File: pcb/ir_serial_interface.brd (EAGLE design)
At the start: 41.9 x 25.4 mm, 33 parts, among them IC1 PIC18LF2550, IC2 LP2992, T1 PS401

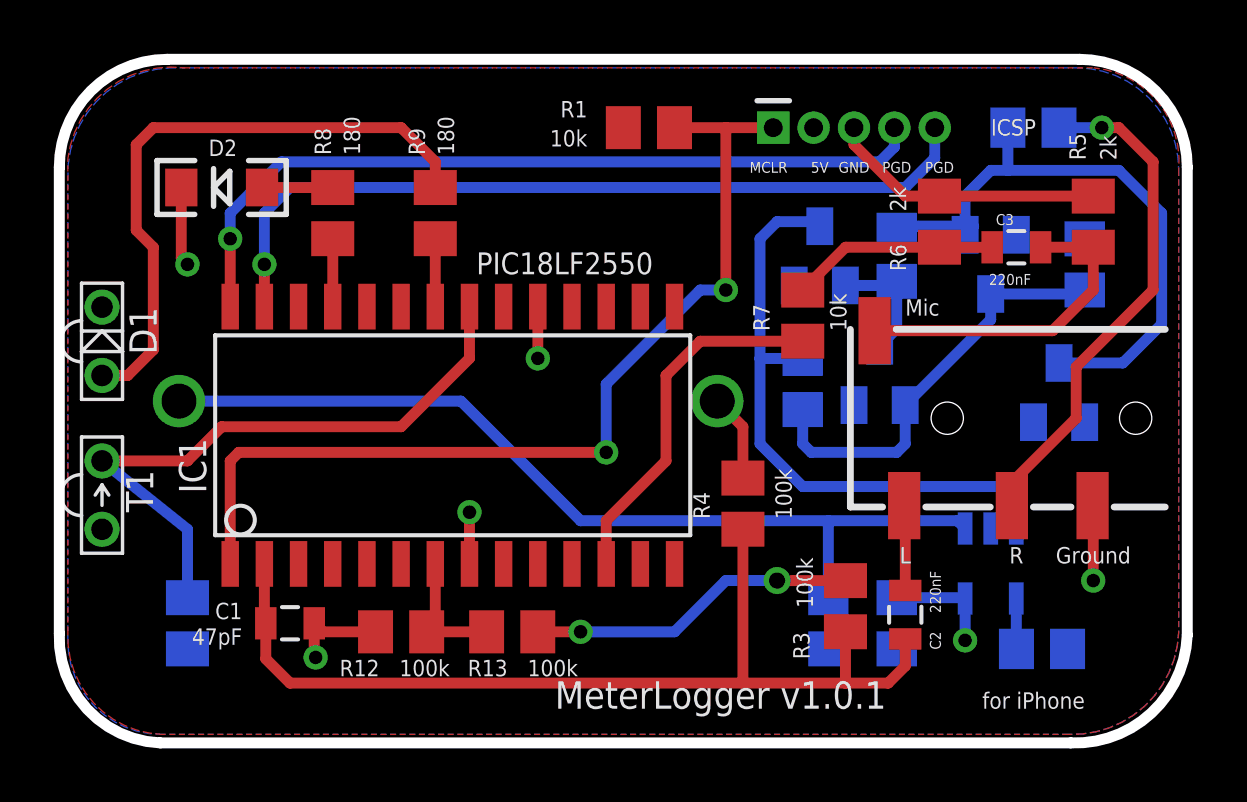
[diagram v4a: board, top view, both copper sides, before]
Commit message: PCB: reuse programmer header for serial debug
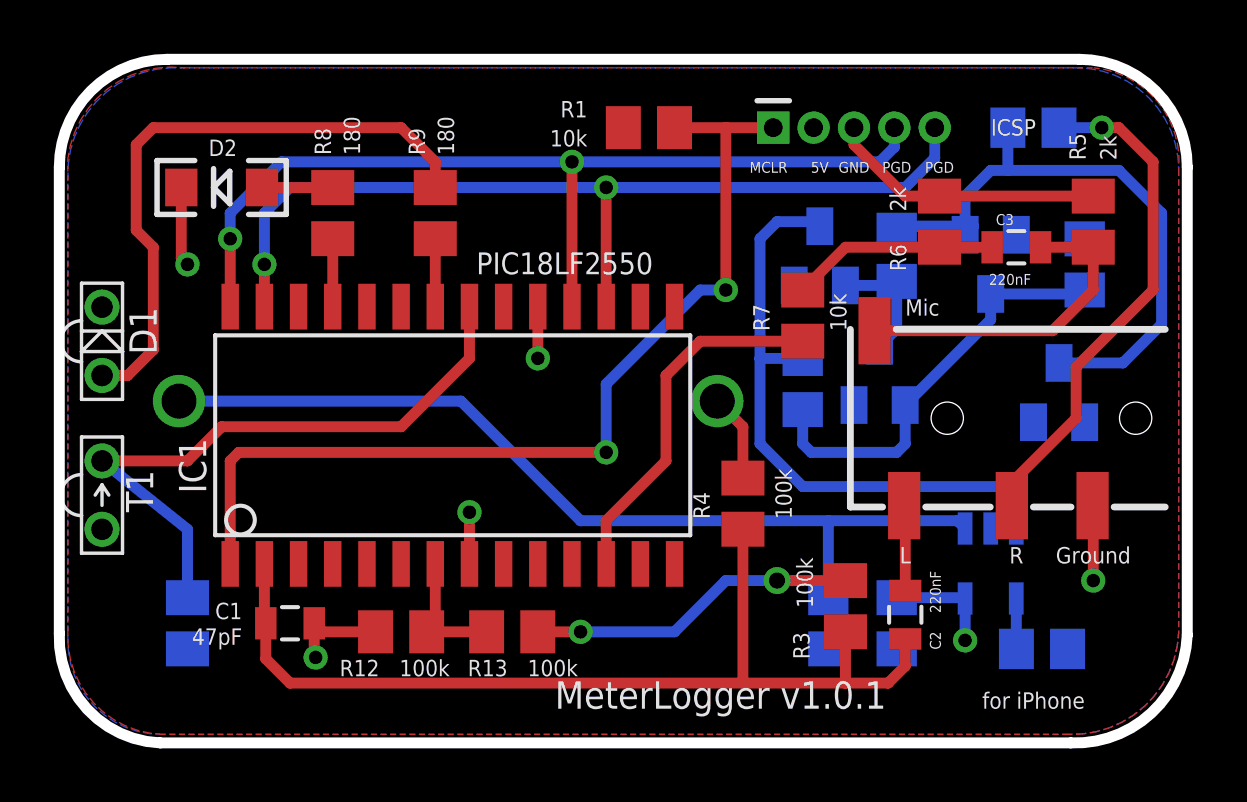
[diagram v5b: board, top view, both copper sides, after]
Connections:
- net N$3: now also IC1.18
- net N$4: now also IC1.17
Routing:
- net N$3: track 29.9 -> 35.3 mm, vias 1 -> 2
- net N$4: track 30.4 -> 34.8 mm, vias 1 -> 2
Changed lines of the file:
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@@
 <setting verticaltext="up"/>
 </settings>
-<grid distance="0.0125" unitdist="inch" unit="inch" style="dots" multiple="1" display="no" altdistance="0.00625" altunitdist="inch" altunit="inch"/>
+<grid distance="0.05" unitdist="inch" unit="inch" style="dots" multiple="1" display="no" altdistance="0.025" altunitdist="inch" altunit="inch"/>
 <layers>
 <layer number="1" name="Top" color="4" fill="1" visible="yes" active="yes"/>
@@
 <wire x1="52.935" y1="48.26" x2="52.935" y2="47.5375" width="0.4064" layer="16"/>
 <wire x1="52.935" y1="47.5375" x2="52.3875" y2="46.99" width="0.4064" layer="16"/>
-<wire x1="52.3875" y1="46.99" x2="30.1625" y2="46.99" width="0.4064" layer="16"/>
+<wire x1="52.3875" y1="46.99" x2="40.9575" y2="46.99" width="0.4064" layer="16"/>
+<wire x1="40.9575" y1="46.99" x2="30.1625" y2="46.99" width="0.4064" layer="16"/>
 <wire x1="30.1625" y1="46.99" x2="28.2575" y2="45.085" width="0.4064" layer="16"/>
 <wire x1="28.2575" y1="45.085" x2="28.2575" y2="44.1325" width="0.4064" layer="16"/>
 <via x="28.2575" y="44.1325" extent="1-16" drill="0.5"/>
 <wire x1="28.2575" y1="41.61" x2="28.2575" y2="44.1325" width="0.4064" layer="1"/>
+<contactref element="IC1" pad="18"/>
+<wire x1="40.9575" y1="41.61" x2="40.9575" y2="46.99" width="0.4064" layer="1"/>
+<via x="40.9575" y="46.99" extent="1-16" drill="0.5"/>
 </signal>
 <signal name="N$4">
@@
 <via x="29.5275" y="43.18" extent="1-16" drill="0.5"/>
 <wire x1="29.5275" y1="43.18" x2="29.5275" y2="41.61" width="0.4064" layer="1"/>
-<wire x1="53.34" y1="46.0375" x2="30.48" y2="46.0375" width="0.4064" layer="16"/>
+<wire x1="53.34" y1="46.0375" x2="42.2275" y2="46.0375" width="0.4064" layer="16"/>
+<wire x1="42.2275" y1="46.0375" x2="30.48" y2="46.0375" width="0.4064" layer="16"/>
 <wire x1="30.48" y1="46.0375" x2="29.5275" y2="45.085" width="0.4064" layer="16"/>
 <wire x1="29.5275" y1="45.085" x2="29.5275" y2="43.18" width="0.4064" layer="16"/>
+<contactref element="IC1" pad="17"/>
+<wire x1="42.2275" y1="41.61" x2="42.2275" y2="46.0375" width="0.4064" layer="1"/>
+<via x="42.2275" y="46.0375" extent="1-16" drill="0.5"/>
 </signal>
 <signal name="N$6">

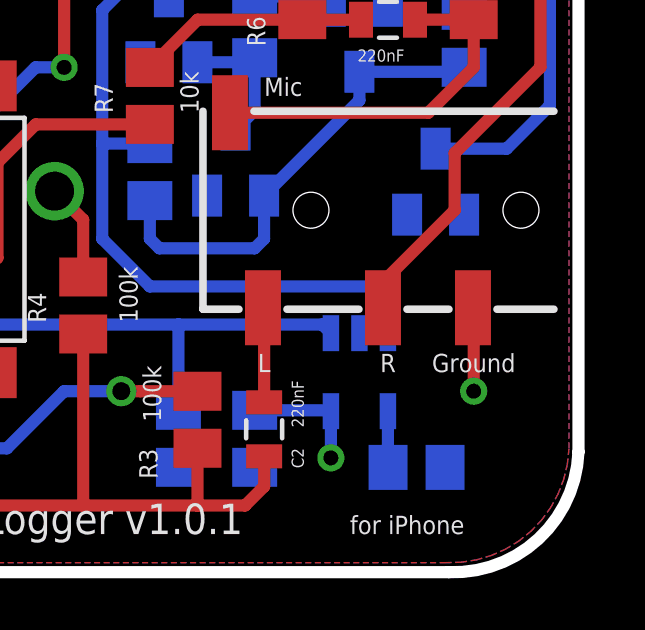
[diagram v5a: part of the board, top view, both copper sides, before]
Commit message: PCB: with zener and serial on ICSP
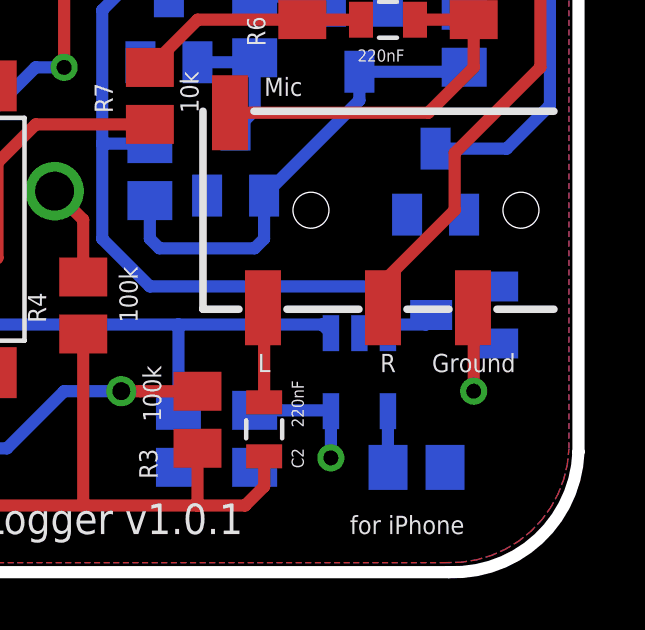
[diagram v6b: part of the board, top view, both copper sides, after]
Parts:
- added D7: MMBZ5231BLT1G, diode:SOT23
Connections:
- net GND: now also D7.1
- net N$21: now also D7.3
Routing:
- net N$21: track 23.3 -> 25.3 mm
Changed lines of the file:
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@@
 <setting verticaltext="up"/>
 </settings>
-<grid distance="0.05" unitdist="inch" unit="inch" style="dots" multiple="1" display="no" altdistance="0.025" altunitdist="inch" altunit="inch"/>
+<grid distance="0.0125" unitdist="inch" unit="inch" style="dots" multiple="1" display="no" altdistance="0.00625" altunitdist="inch" altunit="inch"/>
 <layers>
 <layer number="1" name="Top" color="4" fill="1" visible="yes" active="yes"/>
@@
 <attribute name="VALUE" x="48.26" y="36.195" size="0.6096" layer="26" rot="MR0" align="bottom-right"/>
 </element>
+<element name="D7" library="diode" package="SOT23" value="MMBZ5231BLT1G" x="60.0075" y="33.9725" smashed="yes" rot="MR270">
+<attribute name="NAME" x="58.42" y="34.925" size="0.6096" layer="26" rot="MR90"/>
+<attribute name="VALUE" x="62.23" y="35.56" size="0.6096" layer="26" rot="MR270" align="top-left"/>
+</element>
 </elements>
 <signals>
@@
 <contactref element="D3" pad="1"/>
 <contactref element="C8" pad="1"/>
+<contactref element="D7" pad="1"/>
 <wire x1="54.61" y1="45.7175" x2="53.3425" y2="45.7175" width="0.4064" layer="1"/>
 <wire x1="53.3425" y1="45.7175" x2="51.435" y2="47.625" width="0.4064" layer="1"/>
@@
 <contactref element="D6" pad="3"/>
 <contactref element="IC2" pad="3"/>
+<contactref element="D7" pad="3"/>
+<wire x1="58.9075" y1="33.9725" x2="59.055" y2="33.9725" width="0.4064" layer="16"/>
+<wire x1="59.055" y1="33.9725" x2="58.7375" y2="33.655" width="0.4064" layer="16"/>
+<wire x1="58.7375" y1="33.655" x2="57.7525" y2="33.655" width="0.4064" layer="16"/>
+<wire x1="57.7525" y1="33.655" x2="57.465" y2="33.3675" width="0.4064" layer="16"/>
 <wire x1="57.465" y1="33.3675" x2="57.465" y2="34.61" width="0.4064" layer="16"/>
 <wire x1="57.465" y1="34.61" x2="57.15" y2="34.925" width="0.4064" layer="16"/>
